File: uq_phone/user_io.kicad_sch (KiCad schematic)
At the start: 20 parts, among them J6 503398-1892, J7 Conn_01x02, J8 54132-4062, Q3 MMBT2907ALT1G, U8 LSM6DSVTR, U9 DRV2603RUNR

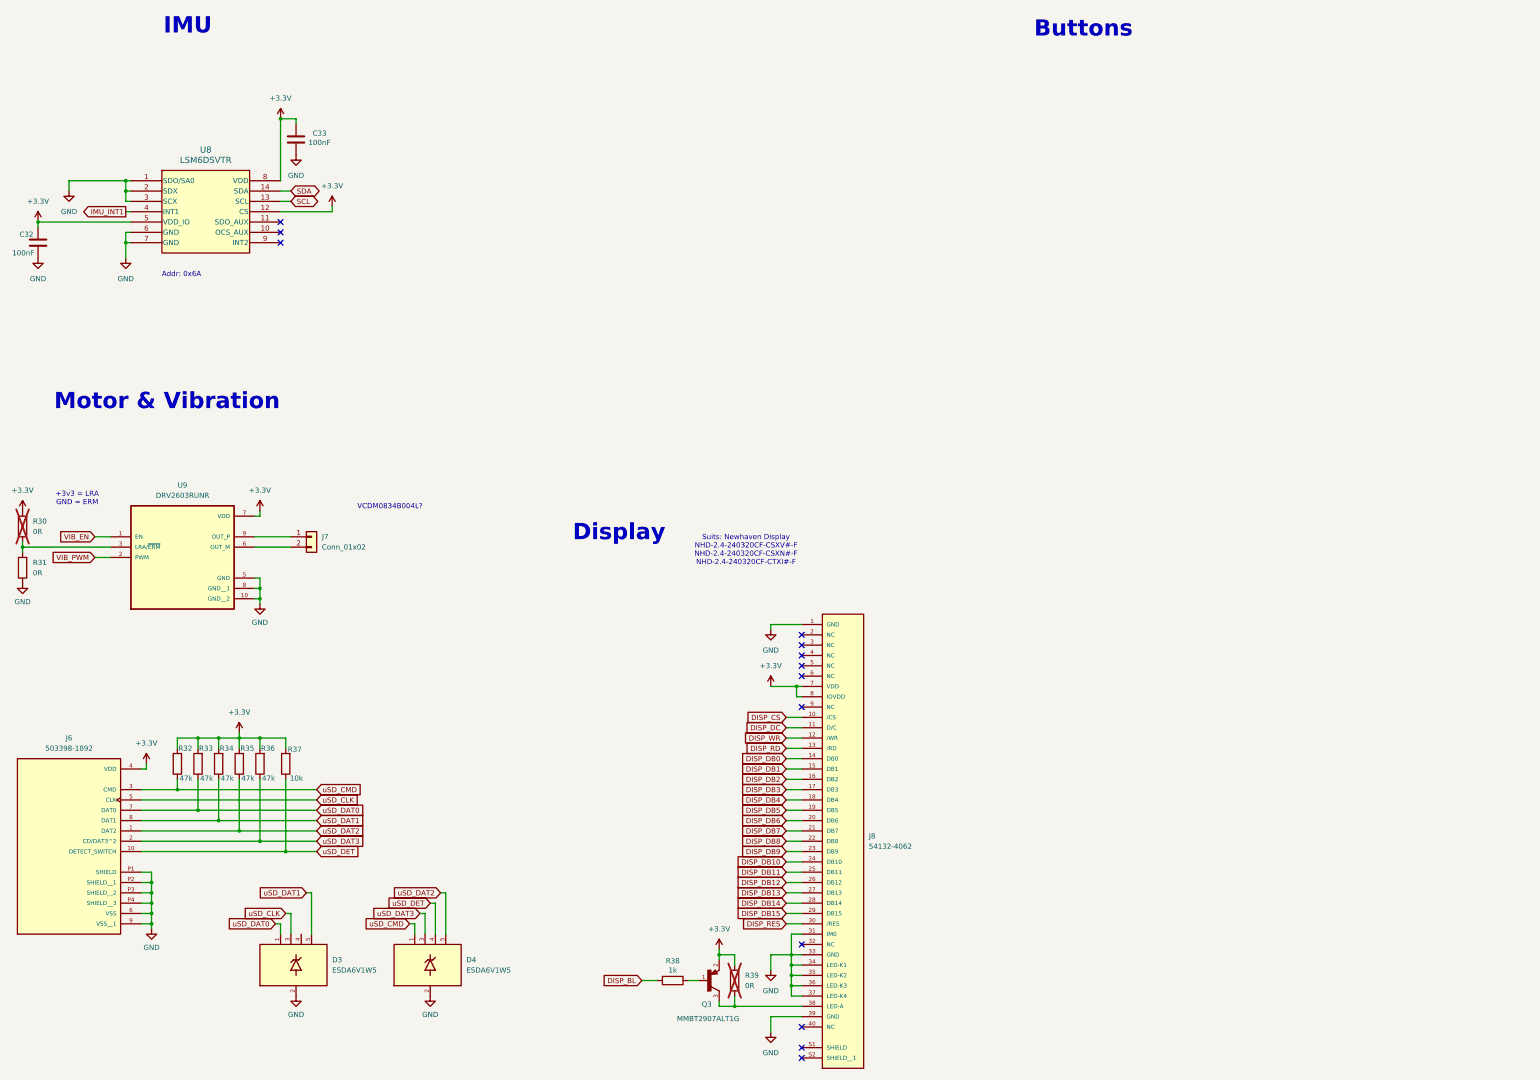
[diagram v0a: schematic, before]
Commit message: Update LCD, Add Programer, Shrink Footprints
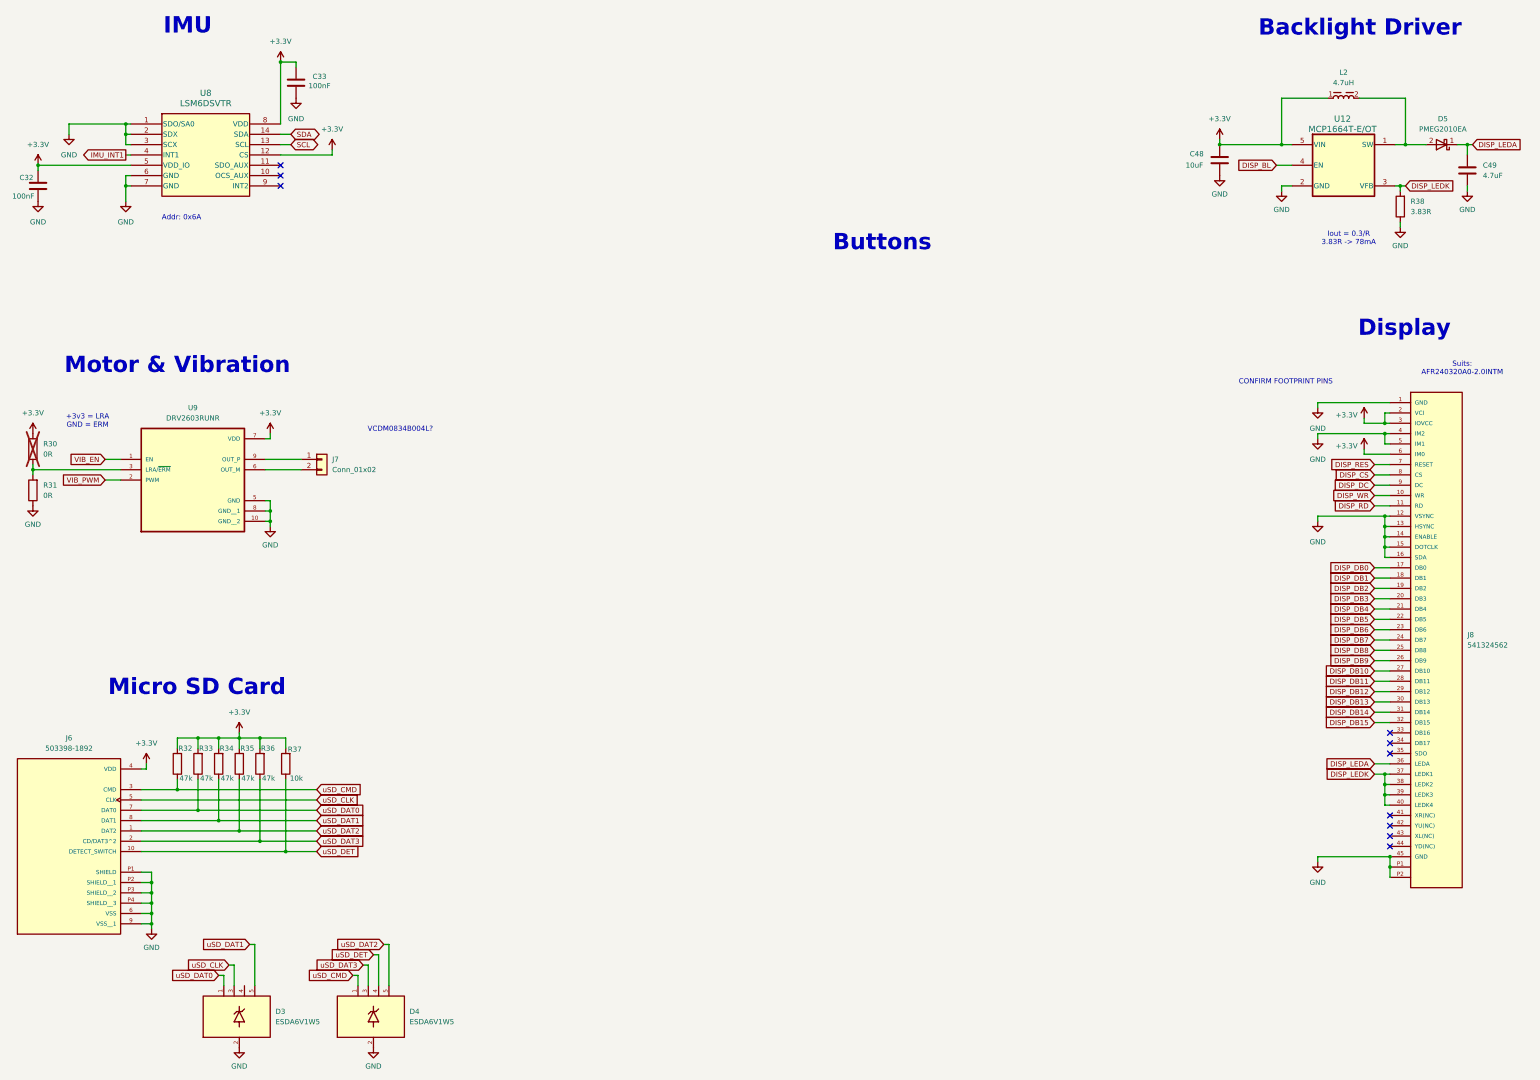
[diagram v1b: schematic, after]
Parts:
- removed J8: 54132-4062, 54132-4062:MOLEX_54132-4062, symbol 54132-4062:54132-4062
- removed Q3: MMBT2907ALT1G, MMBT2907ALT1G:SOT95P240X111-3N, symbol MMBT2907ALT1G:MMBT2907ALT1G
- removed R38: 1k, Resistor_SMD:R_0603_1608Metric, symbol Resistors:Resistor_1k
- removed R39: 0R, Resistor_SMD:R_0603_1608Metric, symbol Resistors:Resistor_0R
- added C48: 10uF, Capacitor_SMD:C_0603_1608Metric, symbol Capacitors:Capacitor_10uF
- added C49: 4.7uF, Capacitor_SMD:C_0603_1608Metric, symbol Capacitors:Capacitor_4.7uF
- added D5: PMEG2010EA, Diode_SMD:D_SOD-323, symbol Misc:PMEG2010EA
- added J8: 541324562, 541324562:CON_541324562_MOL, symbol 541324562:541324562
- added L2: 4.7uH, WE-MAPI_3015:WE-MAPI_3015, symbol WE-MAPI_3015:WE-MAPI_3015
- added R38: 3.83R, Resistor_SMD:R_0603_1608Metric, symbol Resistors:Resistor_3.83R
- added U12: MCP1664T-E/OT, MCP1664T_E_OT:SOT-23-5_OT_MCH, symbol 2025-04-08_10-28-15:MCP1664T-E_OT
- R32, R33, R34, R35, R36, R37: footprint Resistor_SMD:R_0603_1608Metric -> Resistor_SMD:R_0402_1005Metric
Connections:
- net +3.3V: now also C48.1, J8.2 (VCI), J8.3 (IOVCC), J8.6 (IM0), L2.1, U12.5 (VIN)
- net DISP_BL: now also U12.4 (EN)
- net DISP_CS: now also J8.8 (CS)
- net DISP_DB0: now also J8.17 (DB0)
- net DISP_DB1: now also J8.18 (DB1)
- net DISP_DB10: now also J8.27 (DB10)
- net DISP_DB11: now also J8.28 (DB11)
- net DISP_DB12: now also J8.29 (DB12)
- net DISP_DB13: now also J8.30 (DB13)
- net DISP_DB14: now also J8.31 (DB14)
- net DISP_DB15: now also J8.32 (DB15)
- net DISP_DB2: now also J8.19 (DB2)
- net DISP_DB3: now also J8.20 (DB3)
- net DISP_DB4: now also J8.21 (DB4)
- net DISP_DB5: now also J8.22 (DB5)
- net DISP_DB6: now also J8.23 (DB6)
- net DISP_DB7: now also J8.24 (DB7)
- net DISP_DB8: now also J8.25 (DB8)
- net DISP_DB9: now also J8.26 (DB9)
- net DISP_DC: now also J8.9 (DC)
- net DISP_RD: now also J8.11 (RD)
- net DISP_RES: now also J8.7 (RESET)
- net DISP_WR: now also J8.10 (WR)
- net GND: now also C48.2, C49.2, J8.1 (GND), J8.12 (VSYNC), J8.13 (HSYNC), J8.14 (ENABLE), J8.15 (DOTCLK), J8.16 (SDA), J8.4 (IM2), J8.45 (GND), J8.5 (IM1), J8.P1, J8.P2, R38.1, U12.2 (GND)
- new net: D5.2 (A), L2.2, U12.1 (SW)
- new net DISP_LEDA: C49.1, D5.1 (K), J8.36 (LEDA)
- new net DISP_LEDK: J8.37 (LEDK1), J8.38 (LEDK2), J8.39 (LEDK3), J8.40 (LEDK4), R38.2, U12.3 (VFB)
- no-connect marks 13 -> 10
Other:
- note added: "Backlight Driver"
- note added: "CONFIRM FOOTPRINT PINS"
- note added: "Iout = 0.3/R 3.83R -> 78mA"
- note added: "Micro SD Card"
- note added: "Suits: AFR240320A0-2.0INTM"
- note removed: "Suits: Newhaven Display NHD-2.4-240320CF-CSXV#-F NHD-2.4-240320CF-CSXN#-F NHD-2.4-240320CF-CTXI#-F"
- moved on the sheet: C32, C33, D3, D4, J7, R30, R31, U8, U9

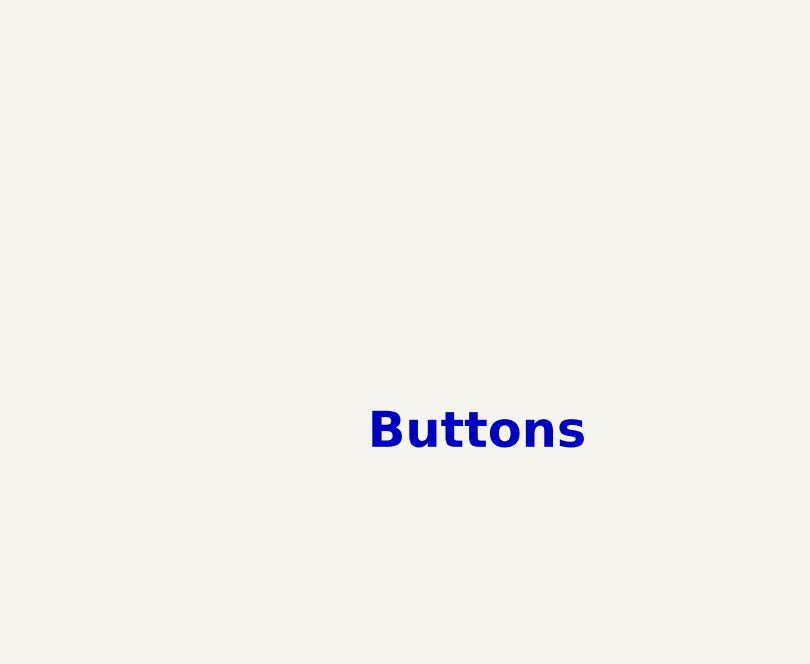
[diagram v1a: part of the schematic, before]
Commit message: Shrink More footprints, rearragment of PCB
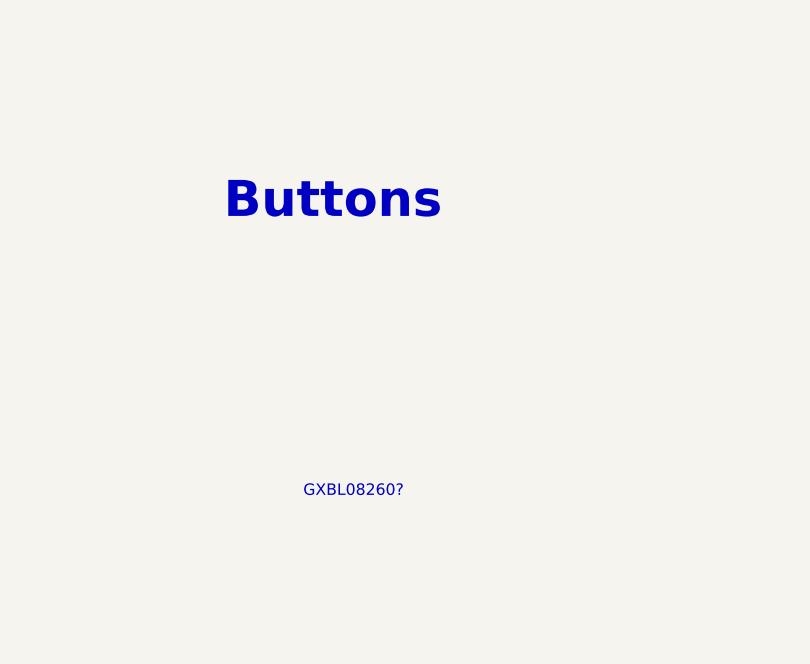
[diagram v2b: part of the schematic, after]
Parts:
- C32, C33, C49: footprint Capacitor_SMD:C_0603_1608Metric -> Capacitor_SMD:C_0402_1005Metric
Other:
- note added: "GXBL08260?"
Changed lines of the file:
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@@
 	(text "Buttons\n"
 		(exclude_from_sim no)
-		(at 230.632 77.47 0)
+		(at 214.63 51.816 0)
 		(effects
 			(font
@@
 		(exclude_from_sim no)
 		(at 329.946 111.76 0)
+		(effects
+			(font
+				(size 1.27 1.27)
+			)
+		)
+	)
+	(text "GXBL08260?"
+		(exclude_from_sim no)
+		(at 216.916 84.074 0)
 		(effects
 			(font
@@
 			)
 		)
-		(property "Description" ""
+		(property "Description" "CAP CER 10UF 6.3V X5R 0603"
 			(at 313.69 57.15 0)
 			(effects
@@
 			)
 		)
-		(property "Footprint" "Capacitor_SMD:C_0603_1608Metric"
+		(property "Footprint" "Capacitor_SMD:C_0402_1005Metric"
 			(at 22.86 63.5 0)
 			(effects
@@
 			)
 		)
-		(property "Description" ""
+		(property "Description" "0.1 µF ±10% 10V Ceramic Capacitor X7R 0402 (1005 Metric)"
 			(at 22.86 63.5 0)
 			(effects
@@
 			)
 		)
-		(property "Footprint" "Capacitor_SMD:C_0603_1608Metric"
+		(property "Footprint" "Capacitor_SMD:C_0402_1005Metric"
 			(at 374.65 59.69 0)
 			(effects
@@
 			)
 		)
-		(property "Description" ""
+		(property "Description" "4.7 µF ±10% 6.3V Ceramic Capacitor X5R 0402 (1005 Metric)"
 			(at 374.65 59.69 0)
 			(effects
@@
 			)
 		)
-		(property "Footprint" "Capacitor_SMD:C_0603_1608Metric"
+		(property "Footprint" "Capacitor_SMD:C_0402_1005Metric"
 			(at 86.36 38.1 0)
 			(effects
@@
 			)
 		)
-		(property "Description" ""
+		(property "Description" "0.1 µF ±10% 10V Ceramic Capacitor X7R 0402 (1005 Metric)"
 			(at 86.36 38.1 0)
 			(effects

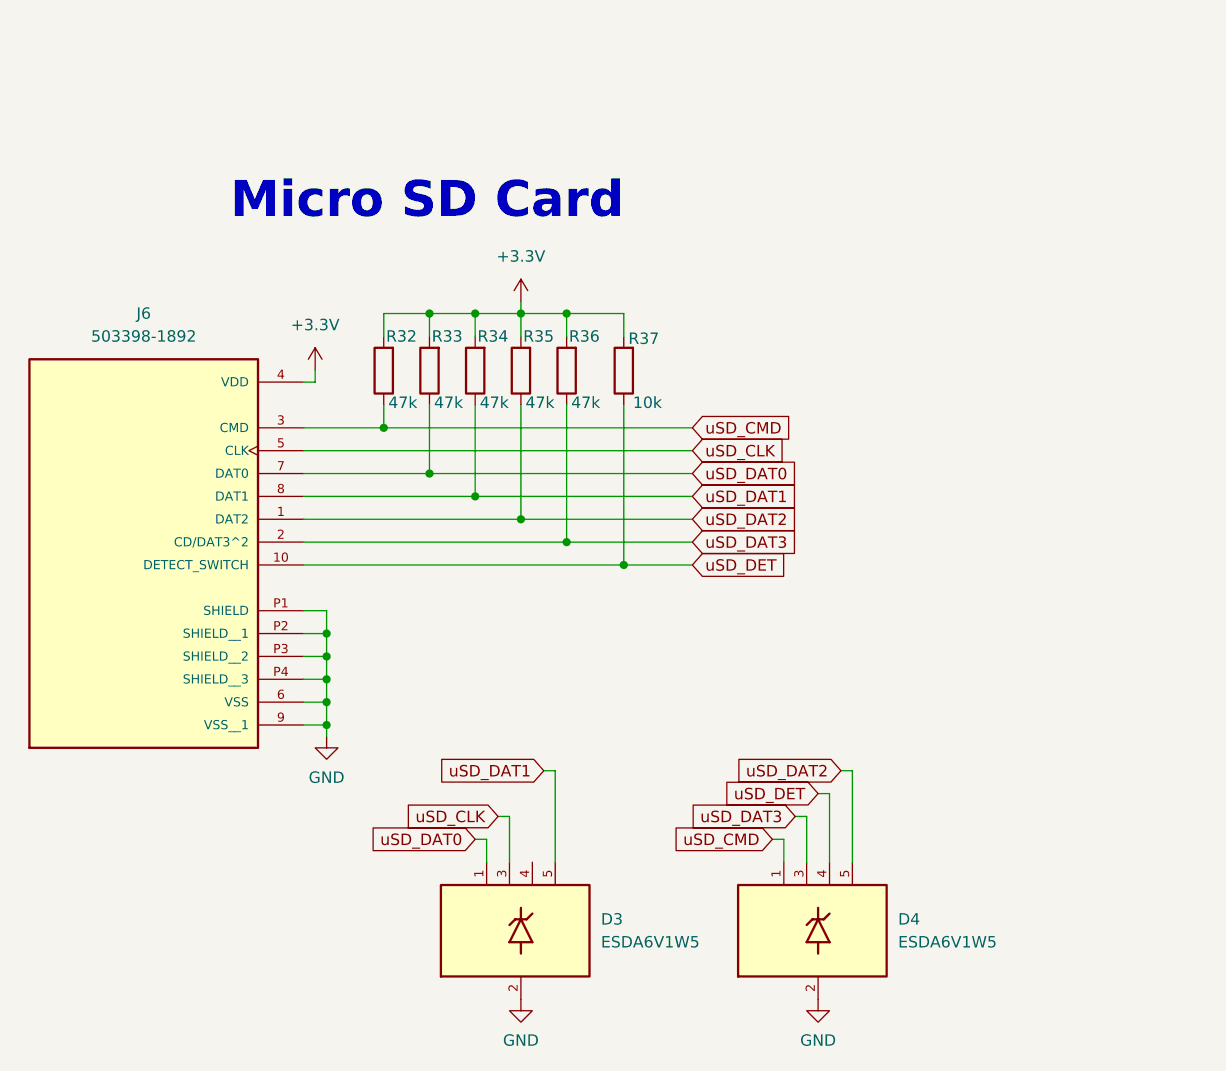
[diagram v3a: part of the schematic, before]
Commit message: Changed SIM/uSD port & adjust routing
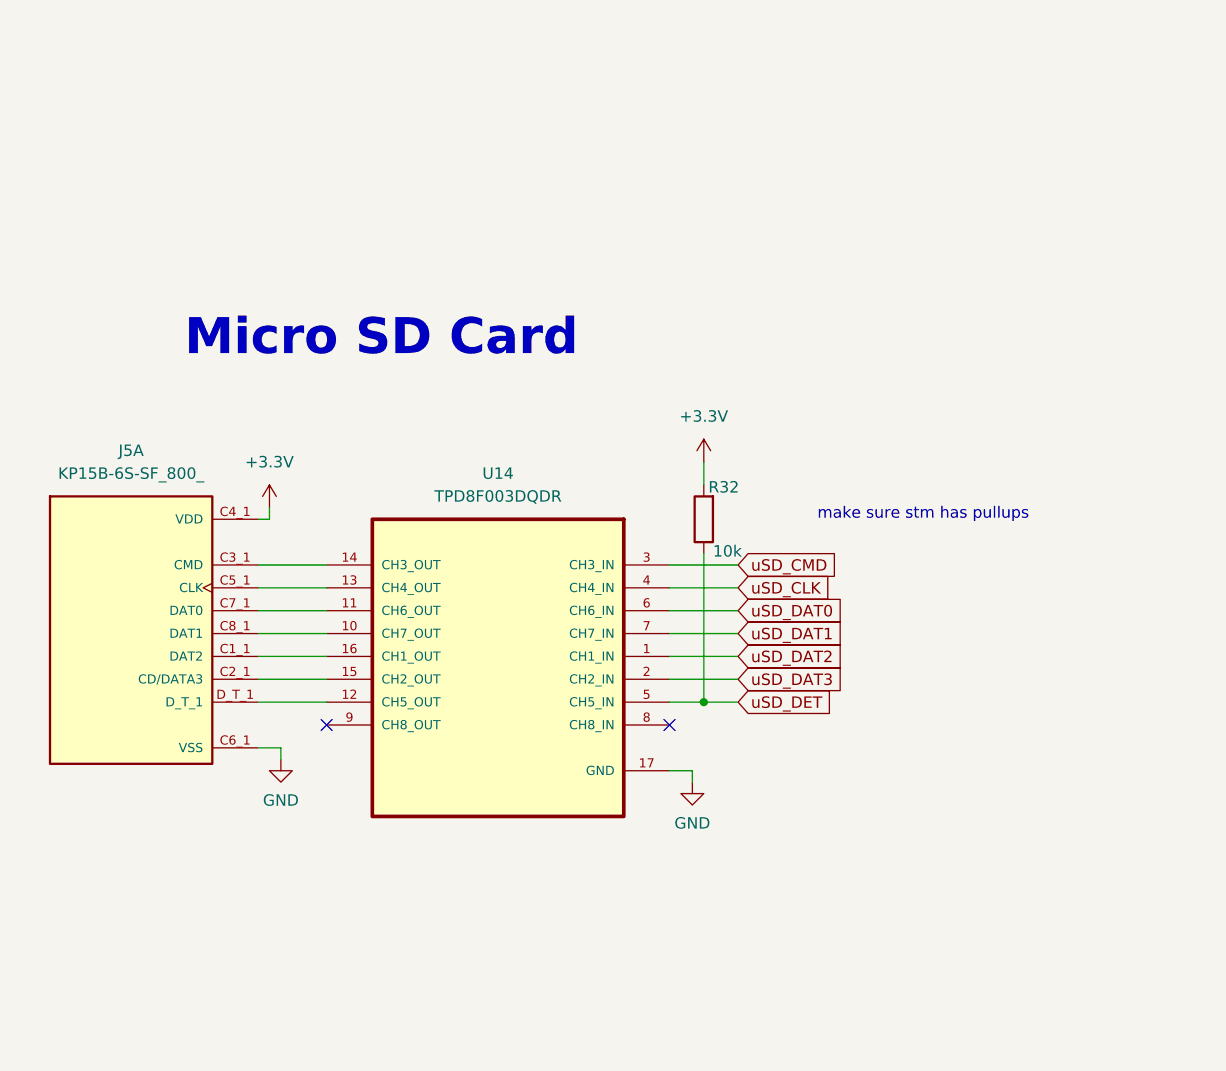
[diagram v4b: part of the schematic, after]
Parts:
- removed D3, D4: ESDA6V1W5, ESDA6V1W5:SOT65P210X110-5N, symbol ESDA6V1W5:ESDA6V1W5
- removed J6: 503398-1892, 503398-1892:MOLEX_503398-1892, symbol 503398-1892:503398-1892
- removed R32, R33, R34, R35, R36: 47k, Resistor_SMD:R_0402_1005Metric, symbol Resistors:Resistor_47k
- removed R37: 10k, Resistor_SMD:R_0402_1005Metric, symbol Resistors:Resistor_10k
- added J5: KP15B-6S-SF_800_, KP15B-6S-SF_800_:HIROSE_KP15B-6S-SF_800_, symbol KP15B-6S-SF_800_:KP15B-6S-SF_800_
- added R32: 10k, Resistor_SMD:R_0402_1005Metric, symbol Resistors:Resistor_10k
- added U14: TPD8F003DQDR, TPD8F003DQDR:SON40P135X330X80-17N, symbol TPD8F003DQDR:TPD8F003DQDR
- J7: footprint Connector_Wire:SolderWire-0.5sqmm_1x02_P4.6mm_D0.9mm_OD2.1mm -> Connector_Wire:SolderWire-0.25sqmm_1x02_P4.2mm_D0.65mm_OD1.7mm
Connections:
- net +3.3V: now also J5.C4_1 (VDD), R32.2
- net GND: now also J5.C6_1 (VSS), U14.17 (GND)
- net uSD_CLK: now also U14.4 (CH4_IN)
- net uSD_CMD: now also U14.3 (CH3_IN)
- net uSD_DAT0: now also U14.6 (CH6_IN)
- net uSD_DAT1: now also U14.7 (CH7_IN)
- net uSD_DAT2: now also U14.1 (CH1_IN)
- net uSD_DAT3: now also U14.2 (CH2_IN)
- net uSD_DET: now also R32.1, U14.5 (CH5_IN)
- new net: J5.C1_1 (DAT2), U14.16 (CH1_OUT)
- new net: J5.C2_1 (CD/DATA3), U14.15 (CH2_OUT)
- new net: J5.C3_1 (CMD), U14.14 (CH3_OUT)
- new net: J5.C5_1 (CLK), U14.13 (CH4_OUT)
- new net: J5.C7_1 (DAT0), U14.11 (CH6_OUT)
- new net: J5.C8_1 (DAT1), U14.10 (CH7_OUT)
- new net: J5.D_T_1, U14.12 (CH5_OUT)
- no-connect marks 10 -> 12
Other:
- note added: "make sure stm has pullups"

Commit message: Arrange PCB
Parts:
- J7: footprint Connector_Wire:SolderWire-0.25sqmm_1x02_P4.2mm_D0.65mm_OD1.7mm -> Connector_Wire:SolderWire-0.15sqmm_1x02_P4mm_D0.5mm_OD1.5mm
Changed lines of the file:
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@@
 			)
 		)
-		(property "Footprint" "Connector_Wire:SolderWire-0.25sqmm_1x02_P4.2mm_D0.65mm_OD1.7mm"
+		(property "Footprint" "Connector_Wire:SolderWire-0.15sqmm_1x02_P4mm_D0.5mm_OD1.5mm"
 			(at 92.71 130.81 0)
 			(effects
